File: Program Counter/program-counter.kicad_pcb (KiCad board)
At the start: 2 copper layers, 63.5 x 45.7 mm, 29 parts, among them J1 Misc, J2 Bus, J3 Power, U1 74LS245, U2 74LS161

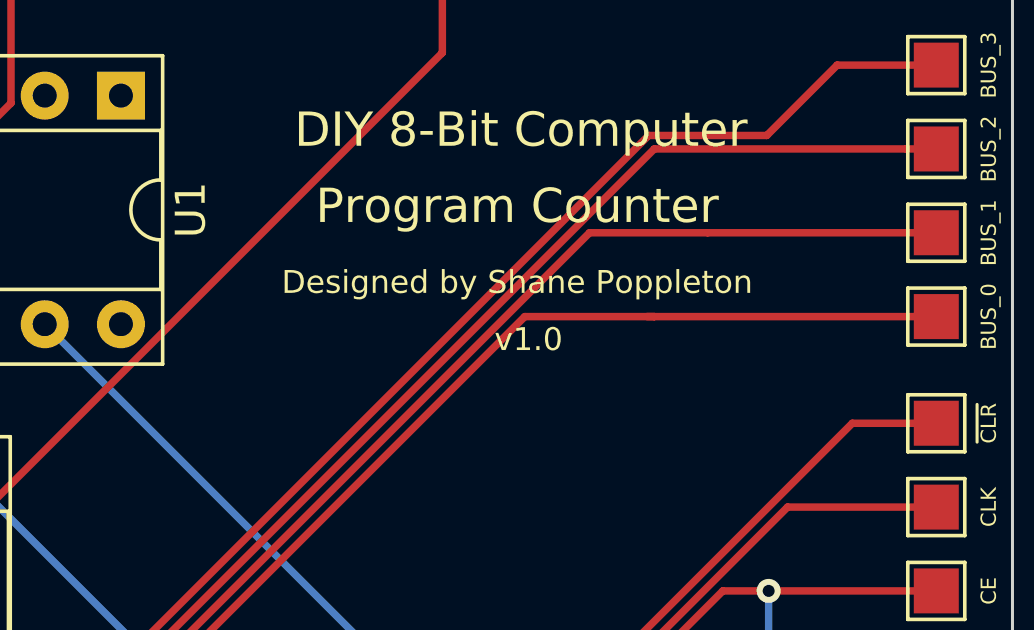
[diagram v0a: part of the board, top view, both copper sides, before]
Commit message: Added Attribution on each PCB, and regenerated gerbers
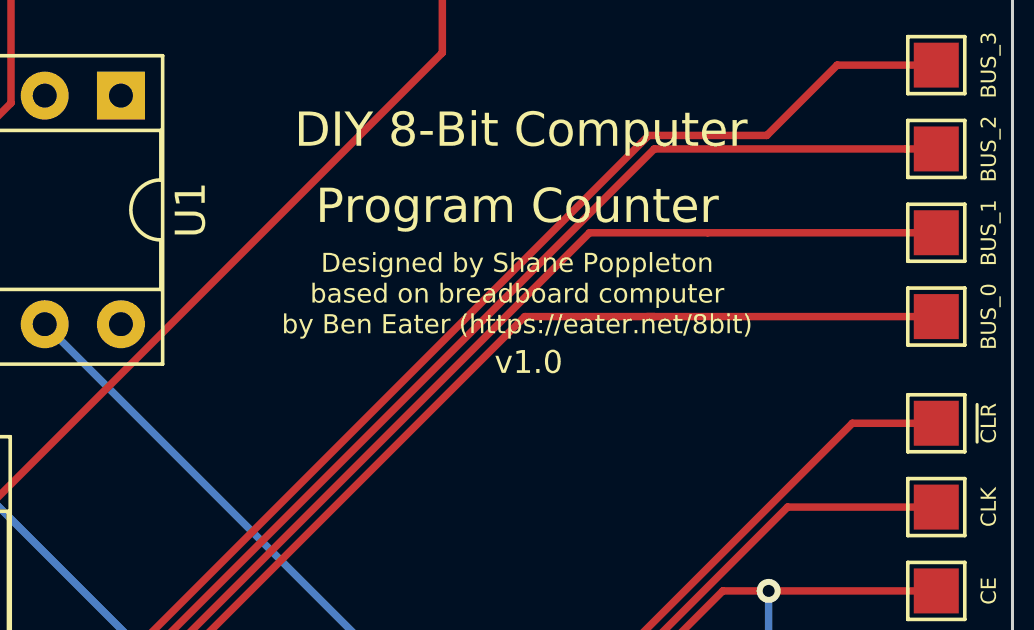
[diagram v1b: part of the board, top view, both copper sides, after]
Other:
- board text added: "Designed by Shane Poppleton based on breadboard computer by Ben Eater (https://eater.net/8bit)"
- board text removed: "Designed by Shane Poppleton"
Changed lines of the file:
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@@
     (effects (font (size 1.143 1.143) (thickness 0.127)))
   )
-  (gr_text v1.0 (at 115.951 96.52) (layer F.SilkS)
+  (gr_text v1.0 (at 115.951 97.282) (layer F.SilkS)
     (effects (font (size 0.762 0.762) (thickness 0.127)))
   )
-  (gr_text "Designed by Shane Poppleton" (at 115.57 94.615) (layer F.SilkS)
-    (effects (font (size 0.762 0.762) (thickness 0.127)))
+  (gr_text "Designed by Shane Poppleton\nbased on breadboard computer\nby Ben Eater (https://eater.net/8bit)\n" (at 115.57 94.996) (layer F.SilkS)
+    (effects (font (size 0.635 0.635) (thickness 0.1016)))
   )
   (gr_text "DIY 8-Bit Computer" (at 115.697 89.535) (layer F.SilkS)
